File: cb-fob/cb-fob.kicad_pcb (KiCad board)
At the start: 4 copper layers, 26.5 x 57.3 mm, 23 parts, among them P1 CONN_01X01, P2 CONN_01X07, SW1 SW_PUSH, SW2 SW_PUSH, SW3 SW_PUSH, SW4 SW_PUSH, U4 MMA8652FC

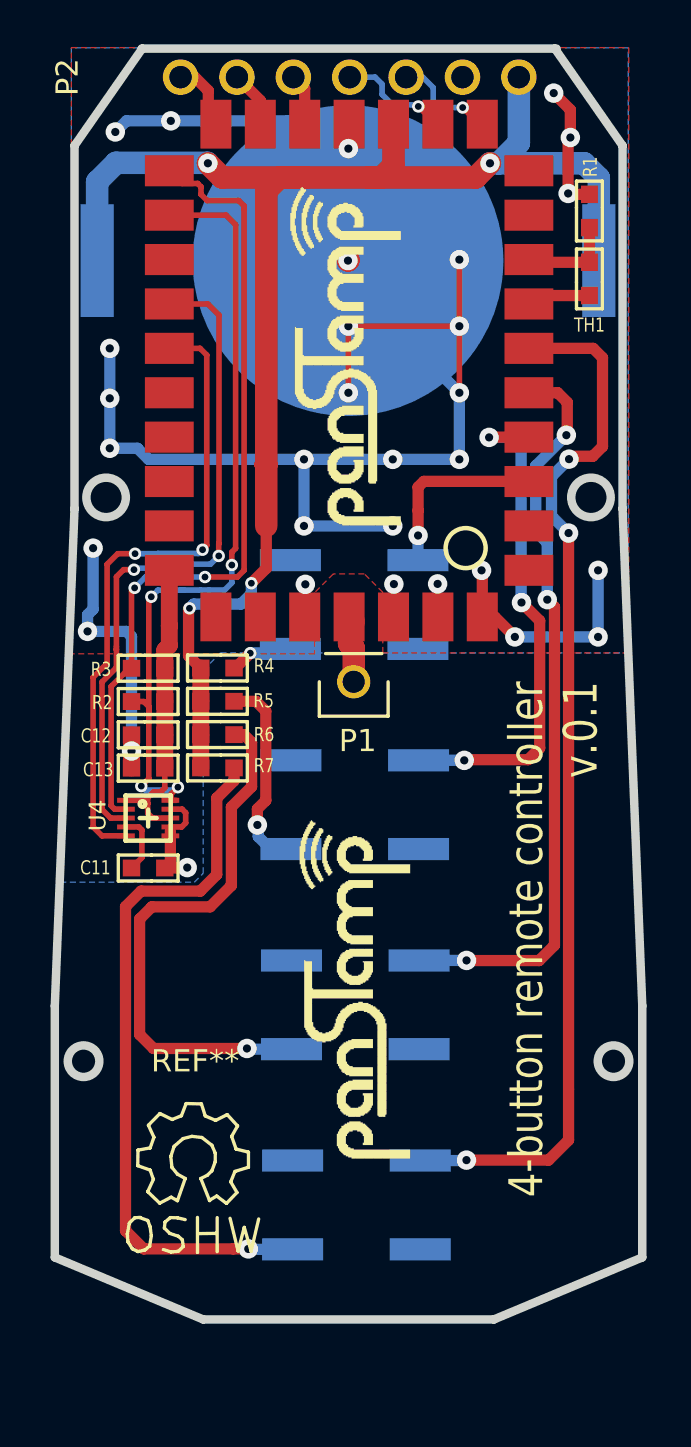
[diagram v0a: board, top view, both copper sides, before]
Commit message: New PCB antenna
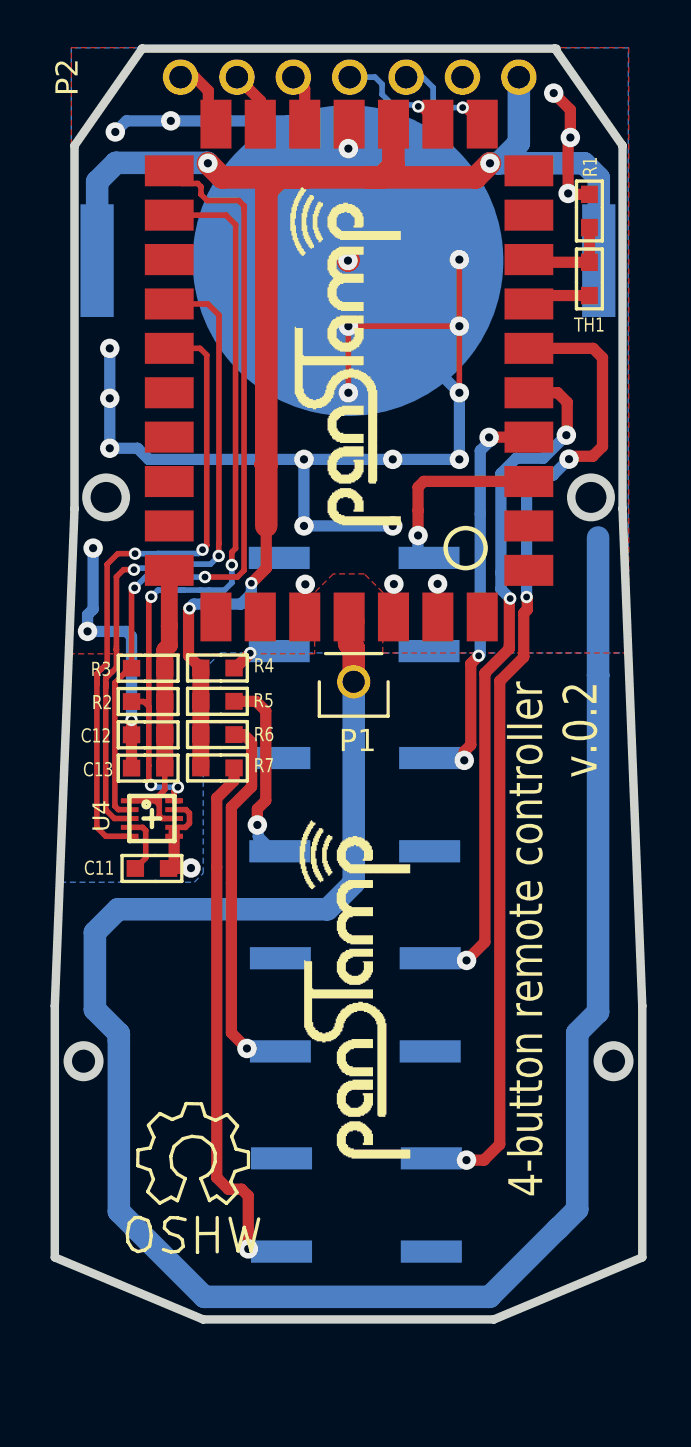
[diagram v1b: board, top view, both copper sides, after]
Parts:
- SW1, SW2, SW3, SW4: footprint Buttons_Switches_SMD:SW_SPST_B3SL-1002P -> mysmd:SW_SPST_PTS645SM
- moved C11 0.17 mm to (74.2, 87.4)
- moved U4 0.17 mm to (74.2, 85.2)
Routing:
- net Net-(P1-Pad1): track 4.18 -> 93.4 mm
- net GND: track 133.1 -> 121.7 mm, vias 31 -> 27
- net Net-(R6-Pad2): track 24.8 -> 17.4 mm
- net Net-(R7-Pad2): track 32.3 -> 24.9 mm
- net /D14: track 23.8 -> 21.2 mm
- net /D12: track 47.6 -> 45.8 mm
- net Net-(R4-Pad2): track 2.89 -> 3.84 mm
- net /D13: track 34.8 -> 34.1 mm
- net /I2C_SDA: track 35.9 -> 35.2 mm
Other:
- board text added: "4-button remote controller v.0.2"
- board text removed: "4-button remote controller v.0.1"
